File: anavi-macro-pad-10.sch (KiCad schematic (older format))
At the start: 21 parts, among them SW1 SW_DIP_x01, SW2 SW_DIP_x01, SW3 SW_DIP_x01, SW4 SW_DIP_x01, SW6 SW_DIP_x01, SW7 SW_DIP_x01, SW8 SW_DIP_x01, U1 SeeeduinoXIAO

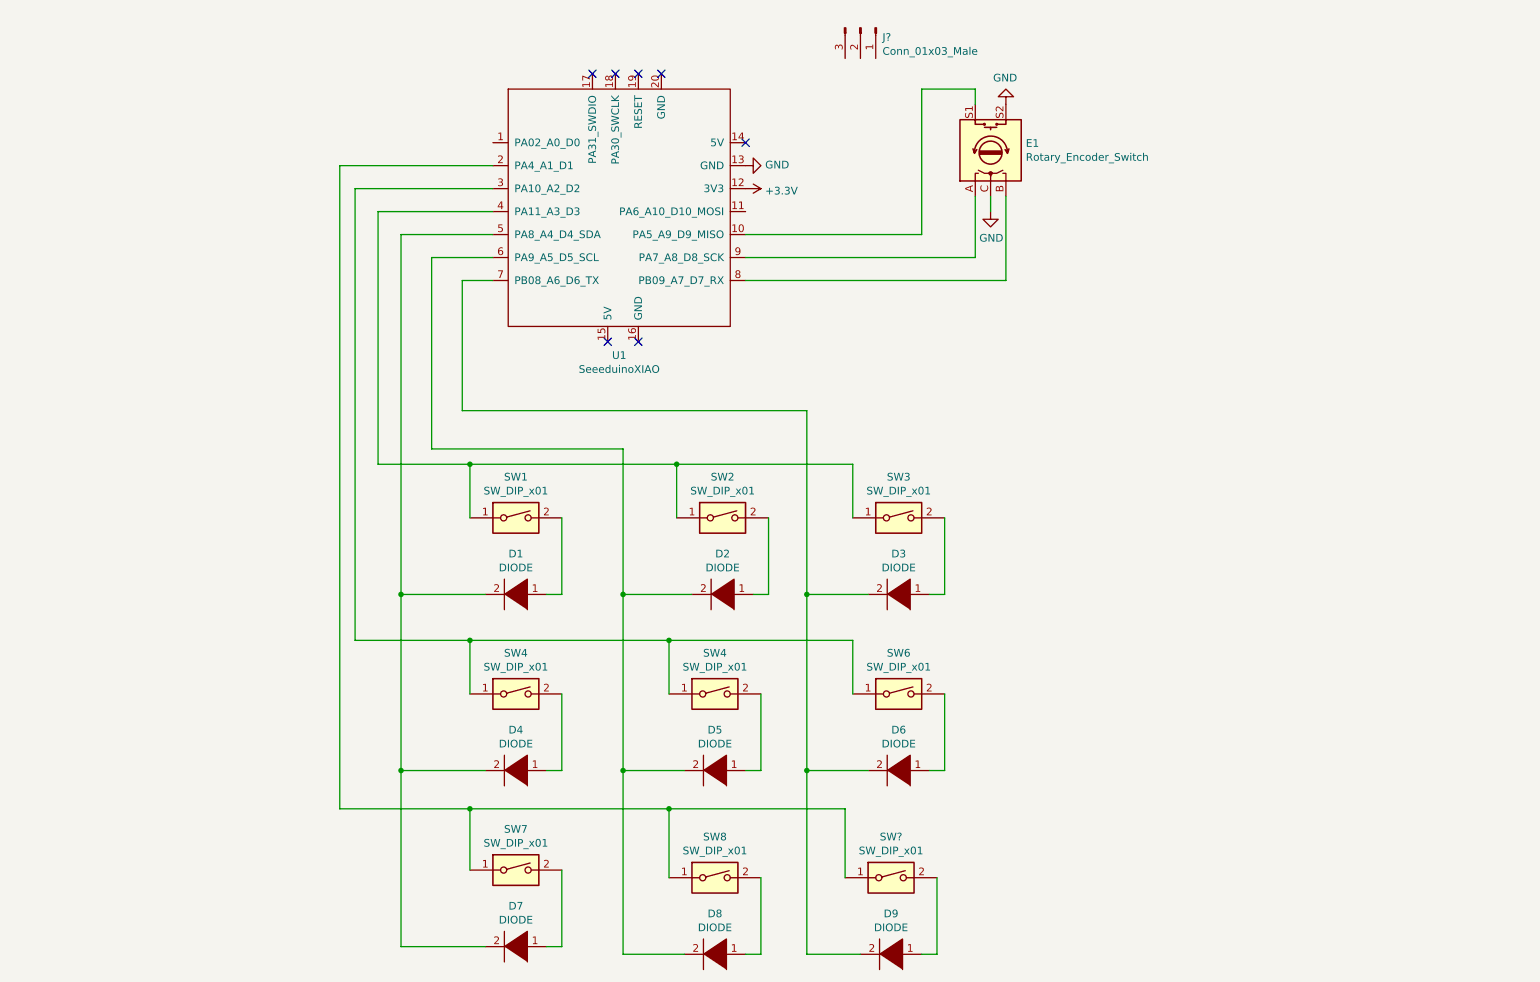
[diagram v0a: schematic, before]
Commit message: anavi-macro-pad-10.sch: Add LEDs
Add LEDs for backlit and underlighting.

Signed-off-by: Leon Anavi <leon@anavi.org>
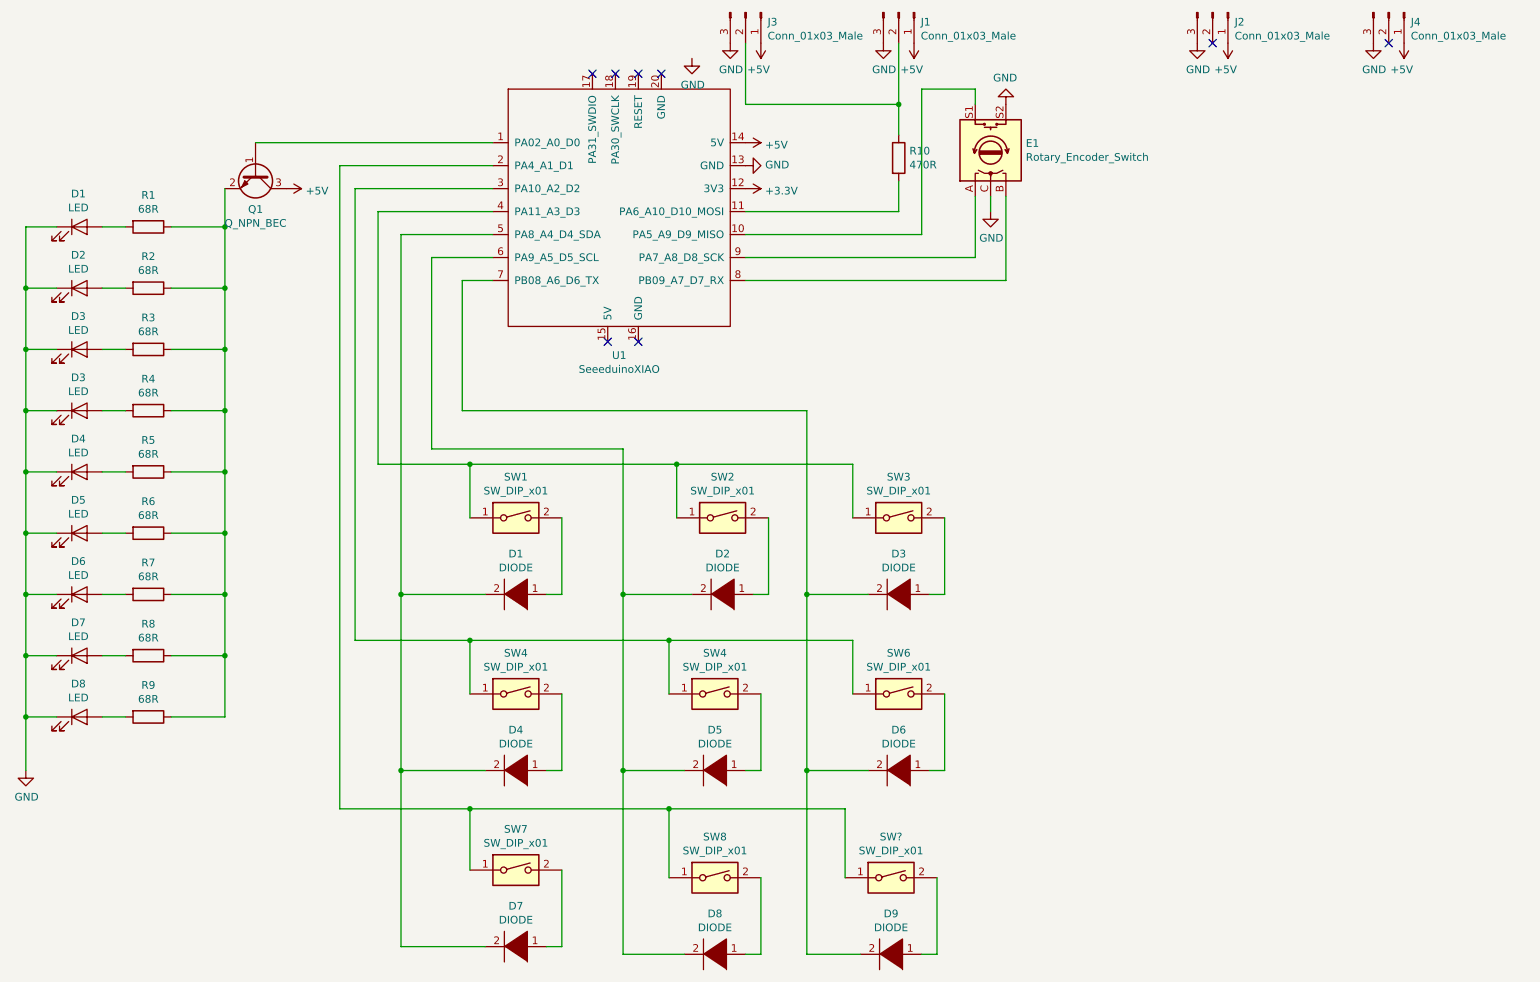
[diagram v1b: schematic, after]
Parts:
- added D1, D2, D3 (x2), D4, D5, D6, D7, D8: LED, LED_SMD:LED_1206_3216Metric, symbol Device:LED
- added J2, J3, J4: Conn_01x03_Male, symbol Connector:Conn_01x03_Male
- added Q1: Q_NPN_BEC, TO_SOT_Packages_SMD:SOT-23, symbol Device:Q_NPN_BEC
- added R1, R2, R3, R4, R5, R6, R7, R8, R9: 68R, Resistors_SMD:R_0603_HandSoldering, symbol Device:R
- added R10: 470R, Resistors_SMD:R_0603_HandSoldering, symbol Device:R
- gave numbers to parts that had none: 1
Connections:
- net GND: now also J1.3 (Pin_3), D1.1 (K), D2.1 (K), D3.1 (K), D3.1 (K), D4.1 (K), D5.1 (K), D6.1 (K), D7.1 (K), D8.1 (K), J2.3 (Pin_3), J3.3 (Pin_3), J4.3 (Pin_3)
- net at U1.1 (PA02_A0_D0): now also Q1.1 (B)
- net at U1.11 (PA6_A10_D10_MOSI): now also R10.2
- net +5V: now reaches U1.14 (5V)
- net +5V: now also J1.1 (Pin_1), J2.1 (Pin_1), J3.1 (Pin_1), J4.1 (Pin_1), Q1.3 (C)
- net at J1.2 (Pin_2): now also J3.2 (Pin_2), R10.1
- new net: Q1.2 (E), R1.1, R2.1, R3.1, R4.1, R5.1, R6.1, R7.1, R8.1, R9.1
- new net: D1.2 (A), R1.2
- new net: D2.2 (A), R2.2
- new net: D3.2 (A), R3.2
- new net: D3.2 (A), R4.2
- new net: D4.2 (A), R5.2
- new net: D5.2 (A), R6.2
- new net: D6.2 (A), R7.2
- new net: D7.2 (A), R8.2
- new net: D8.2 (A), R9.2
- no-connect marks 7 -> 8
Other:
- moved on the sheet: J1

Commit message: anavi-macro-pad-10: Create PCB
Create printed circuit board.

Signed-off-by: Leon Anavi <leon@anavi.org>
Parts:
- D1: value DIODE -> 1N4148; footprint (none) -> Diode_SMD:D_SOD-123
- D2, D3, D4, D5, D6, D7, D8, D9: footprint (none) -> Diode_SMD:D_SOD-123
- J1, J2, J3, J4: footprint (none) -> led:LedConnector_1x03_P2.54mm
- SW1, SW2, SW3, SW4, SW6, SW7, SW8: footprint (none) -> keyswitches:Kailh_socket_MX
- SW5: renamed from SW4; footprint (none) -> keyswitches:Kailh_socket_MX
- SW9: renamed from SW?; footprint (none) -> keyswitches:Kailh_socket_MX
- renumbered D1 to L1, D2 to L2, D3 to L3, D3 to L4, D4 to L5, D5 to L6, D6 to L7, D7 to L8, D8 to L9
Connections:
- net at J1.2 (Pin_2), R10.1: no longer J3.2 (Pin_2)
- net at J2.2 (Pin_2): now also J3.2 (Pin_2)
- no-connect marks 8 -> 7
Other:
- moved on the sheet: J2, J3, J4
